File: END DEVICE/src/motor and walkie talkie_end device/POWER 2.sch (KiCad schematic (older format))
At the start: 29 parts, among them IC4 TPS55340RTER, SW6 SW_SPDT, U6 LM1117-3.3(, U9 L4931ABDT50

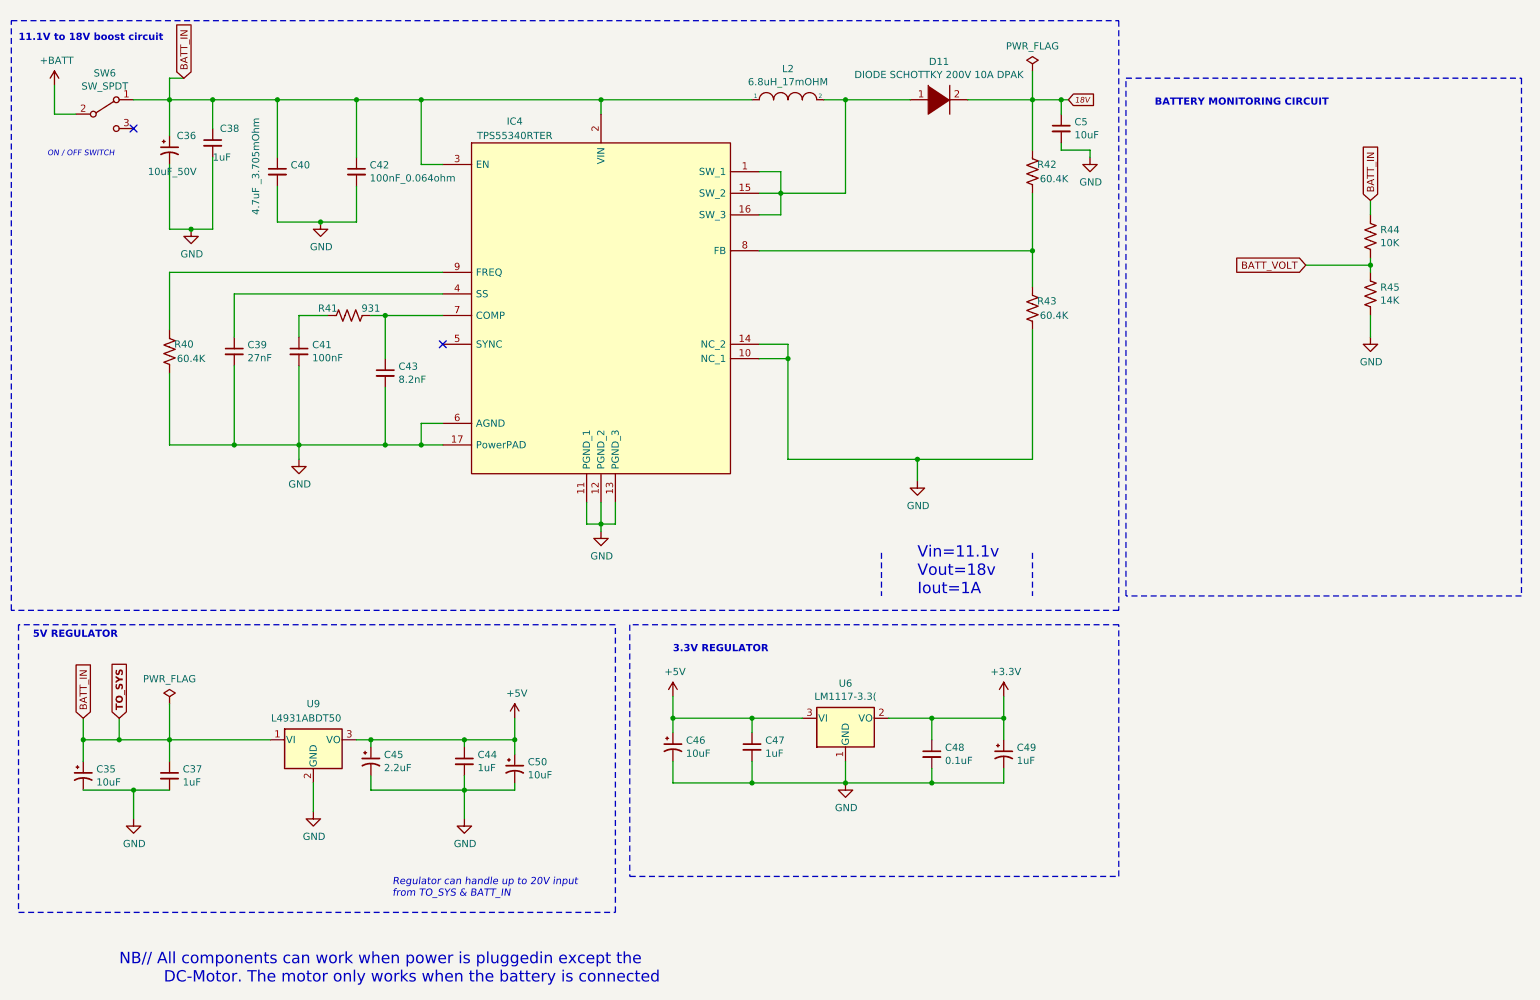
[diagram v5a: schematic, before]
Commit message: Version 2 compressed board
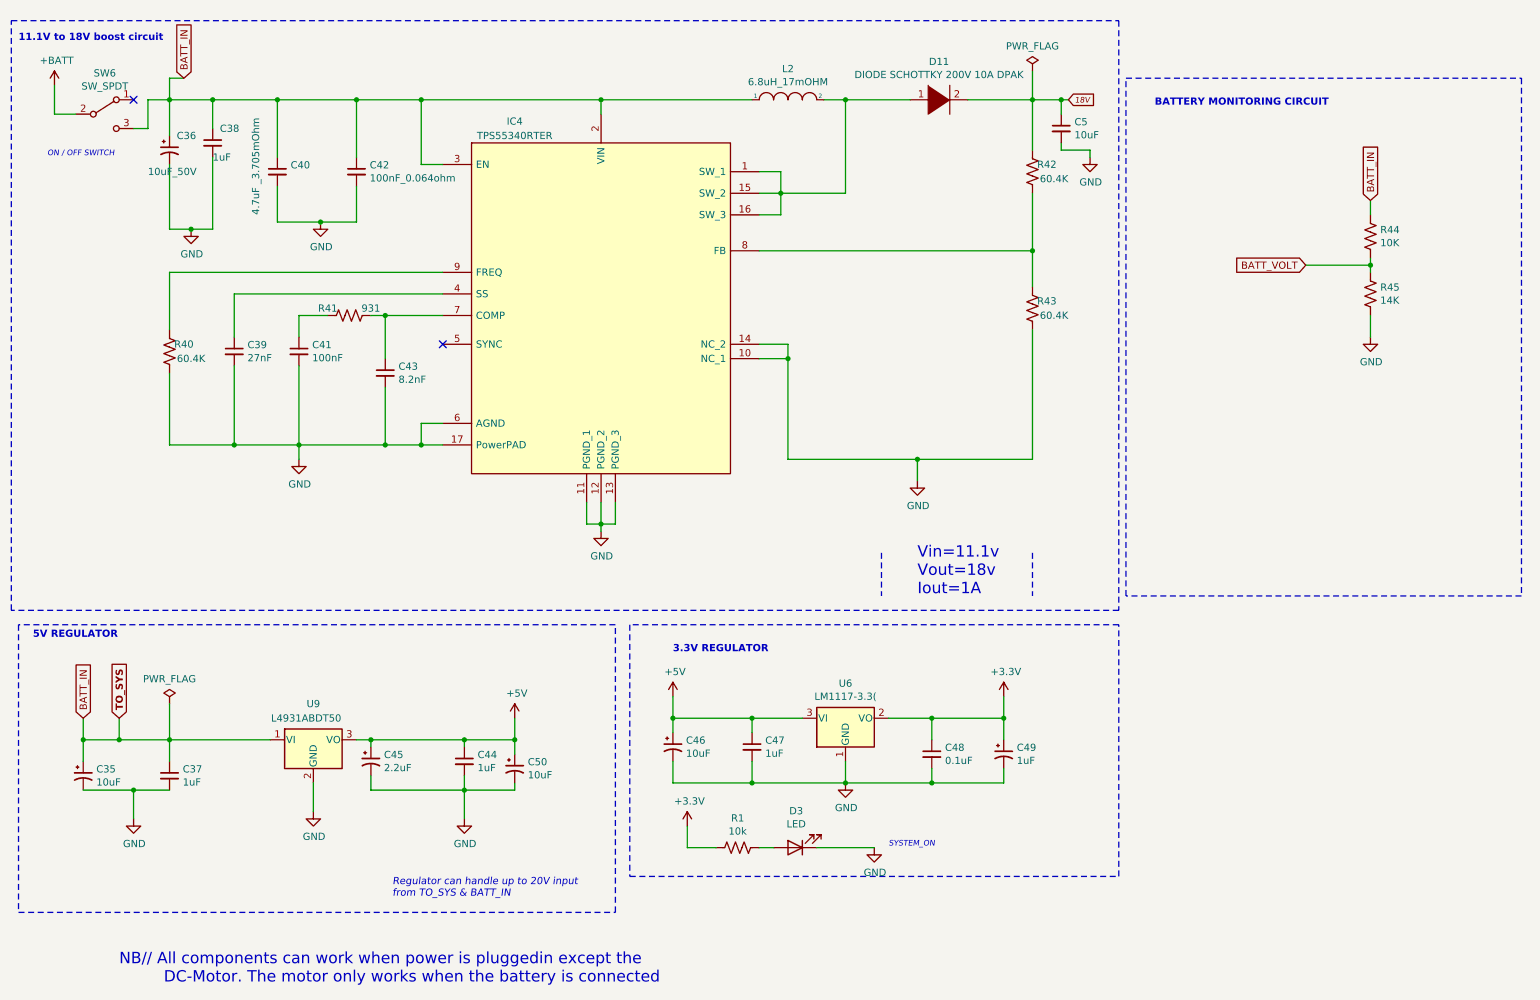
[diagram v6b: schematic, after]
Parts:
- added D3: LED, LED_SMD:LED_0603_1608Metric, symbol Device:LED
- added R1: 10k, Resistor_SMD:R_0603_1608Metric, symbol Device:R_US
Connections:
- net +3V3: now also R1.2
- net BATT_IN: now also SW6.3 (C); no longer SW6.1 (A)
- net GND: now also D3.1 (K)
- new net: D3.2 (A), R1.1
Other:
- note added: "SYSTEM_ON"
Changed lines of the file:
@@
 Wire Wire Line
 	3000 1100 3450 1100
-Wire Wire Line
-	1450 1100 1700 1100
 $Comp
 L Device:C_Small C38
@@
 Wire Wire Line
 	7700 900  7700 1100
-NoConn ~ 1450 1300
+NoConn ~ 1450 1100
 Wire Notes Line
 	8350 950  11100 950
@@
 Wire Wire Line
 	7900 1100 7700 1100
+$Comp
+L Device:R_US R?
+U 1 1 61329130
+P 5650 6300
+AR Path="/615FCEB9/61329130" Ref="R?"  Part="1"
+AR Path="/61DE992E/61329130" Ref="R?"  Part="1"
+AR Path="/61DF39DA/61329130" Ref="R1"  Part="1"
+F 0 "R1" V 5445 6300 50  0000 C CNN
+F 1 "10k" V 5536 6300 50  0000 C CNN
+F 2 "Resistor_SMD:R_0603_1608Metric" V 5690 6290 50  0001 C CNN
+F 3 "~" H 5650 6300 50  0001 C CNN
+	1    5650 6300
+	0    1    1    0
+$EndComp
+$Comp
+L Device:LED D?
+U 1 1 61329138
+P 6050 6300
+AR Path="/615FCEB9/61329138" Ref="D?"  Part="1"
+AR Path="/61DE992E/61329138" Ref="D?"  Part="1"
+AR Path="/61DF39DA/61329138" Ref="D3"  Part="1"
+F 0 "D3" H 6043 6045 50  0000 C CNN
+F 1 "LED" H 6043 6136 50  0000 C CNN
+F 2 "LED_SMD:LED_0603_1608Metric" H 6050 6300 50  0001 C CNN
+F 3 "~" H 6050 6300 50  0001 C CNN
+	1    6050 6300
+	-1   0    0    1
+$EndComp
+Wire Wire Line
+	5900 6300 5800 6300
+Text Notes 6700 6300 0    39   Italic 0
+SYSTEM_ON
+$Comp
+L power:GND #PWR04
+U 1 1 61338120
+P 6600 6300
+F 0 "#PWR04" H 6600 6050 50  0001 C CNN
+F 1 "GND" H 6605 6127 50  0000 C CNN
+F 2 "" H 6600 6300 50  0001 C CNN
+F 3 "" H 6600 6300 50  0001 C CNN
+	1    6600 6300
+	1    0    0    -1
+$EndComp
+Wire Wire Line
+	6200 6300 6600 6300
+$Comp
+L power:+3.3V #PWR03
+U 1 1 61347035
+P 5300 6150
+F 0 "#PWR03" H 5300 6000 50  0001 C CNN
+F 1 "+3.3V" H 5315 6323 50  0000 C CNN
+F 2 "" H 5300 6150 50  0001 C CNN
+F 3 "" H 5300 6150 50  0001 C CNN
+	1    5300 6150
+	1    0    0    -1
+$EndComp
+Wire Wire Line
+	5300 6150 5300 6300
+Wire Wire Line
+	5300 6300 5500 6300
+Wire Wire Line
+	1700 1100 1550 1100
+Wire Wire Line
+	1550 1100 1550 1300
+Wire Wire Line
+	1550 1300 1450 1300
 $EndSCHEMATC

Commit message: latest update
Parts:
- L2: footprint Remote_devices:SDR1307680KL -> Remote_devices:ASPI-7318-6R8M-T; Mfr No. SDR1307-6R8ML -> ASPI-7318-6R8M-T
- R44: value 10K -> 28.2k
- R45: value 14K -> 10
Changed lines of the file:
@@
 F 0 "L2" H 6000 1315 50  0000 C CNN
 F 1 "6.8uH_17mOHM" H 6000 1224 50  0000 C CNN
-F 2 "Remote_devices:SDR1307680KL" H 6000 1100 50  0001 C CNN
+F 2 "Remote_devices:ASPI-7318-6R8M-T" H 6000 1100 50  0001 C CNN
 F 3 "~" H 6000 1100 50  0001 C CNN
 F 4 "Bourns" H 6000 1100 50  0001 C CNN "Mfr"
-F 5 "SDR1307-6R8ML" H 6000 1100 50  0001 C CNN "Mfr No."
+F 5 "ASPI-7318-6R8M-T" H 6000 1100 50  0001 C CNN "Mfr No."
 	1    6000 1100
 	1    0    0    -1
@@
 P 10050 2050
 F 0 "R44" H 10118 2096 50  0000 L CNN
-F 1 "10K" H 10118 2005 50  0000 L CNN
+F 1 "28.2k" H 10118 2005 50  0000 L CNN
 F 2 "Resistor_SMD:R_0603_1608Metric" V 10090 2040 50  0001 C CNN
 F 3 "~" H 10050 2050 50  0001 C CNN
@@
 P 10050 2450
 F 0 "R45" H 10118 2496 50  0000 L CNN
-F 1 "14K" H 10118 2405 50  0000 L CNN
+F 1 "10" H 10118 2405 50  0000 L CNN
 F 2 "Resistor_SMD:R_0603_1608Metric" V 10090 2440 50  0001 C CNN
 F 3 "~" H 10050 2450 50  0001 C CNN

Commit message: 90% complete and. PCB done with tracks and design rules verified as well as dimensions
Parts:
- C35: footprint Capacitor_SMD:CP_Elec_4x4.5 -> Capacitor_Tantalum_SMD:CP_EIA-6032-28_Kemet-C; Mfr No. (none) -> T491C106K035AT; Supplier (none) -> LCSC
- C36: value 10uF_50V -> 10uF_>30V; footprint Capacitor_Tantalum_SMD:CP_EIA-1608-08_AVX-J -> Capacitor_Tantalum_SMD:CP_EIA-6032-28_Kemet-C; Mfr No. (none) -> T491C106K035AT; Supplier (none) -> LCSC
- C45: footprint Capacitor_Tantalum_SMD:CP_EIA-2012-12_Kemet-R_Pad1.30x1.05mm_HandSolder -> Capacitor_Tantalum_SMD:CP_EIA-7343-31_Kemet-D
- C46: footprint Capacitor_Tantalum_SMD:CP_EIA-2012-12_Kemet-R_Pad1.30x1.05mm_HandSolder -> Capacitor_Tantalum_SMD:CP_EIA-6032-28_Kemet-C; Mfr No. (none) -> T491C106K035AT; Suppier (none) -> Digikey
- C49: footprint Capacitor_Tantalum_SMD:CP_EIA-2012-12_Kemet-R_Pad1.30x1.05mm_HandSolder -> Capacitor_Tantalum_SMD:CP_EIA-3216-18_Kemet-A; Mfr No. (none) -> T498A105K016ATE6K5; Supplier (none) -> Digikey
- C50: footprint Capacitor_Tantalum_SMD:CP_EIA-2012-12_Kemet-R_Pad1.30x1.05mm_HandSolder -> Capacitor_Tantalum_SMD:CP_EIA-6032-28_Kemet-C; Mfr No. (none) -> T491C106K035AT; Supplier (none) -> LCSC
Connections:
- net +BATT: no longer SW6.2 (B)
- net BATT_VOLT renamed BATT_VOLTAGE
- new net TO_SYS: SW6.2 (B)
- no-connect marks 2 -> 3
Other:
- note added: "Correction. the BATT+ connection should be remves and the TO-SYS be used as imput to the system only!"
- note added: "POWER_ON LED"
- note added: "the previous design disconnects the battery only when its switch off but does not disconnect the system when powered via an external source."
- note removed: "NB// All components can work when power is pluggedin except the\n DC-Motor. The motor only works when the battery is connected"
- moved on the sheet: C5, D3, R1, R42, R43
